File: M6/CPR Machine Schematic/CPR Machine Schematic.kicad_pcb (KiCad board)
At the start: 2 copper layers, 79.8 x 56.3 mm, 72 parts, among them J1 Battery 22.2V IN, J10 Stop Button Port, J11 Go Button Port, J12 I2C Port, J13 Raspberry_Pi_2_3, J2 5V Spare Headers, J3 Power Switch, J4 3V3 Spare Headers, J5 12 Spare headers, J6 Battery Spare headers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

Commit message: Final PCB
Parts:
- removed the REF** at (118.6, 76.0)
- removed the REF** at (176.6, 125.0)
- removed the REF** at (118.6, 125.0)
- removed the REF** at (176.6, 76.0)
- added G***: LOGO, Images:MIT, F.Cu at (149.6, 89.2)
- added H1: MountingHole, MountingHole:MountingHole_2.7mm_M2.5_Pad, F.Cu at (176.6, 76.0)
- added H2: MountingHole, MountingHole:MountingHole_2.7mm_M2.5_Pad, F.Cu at (176.6, 125.0)
- added H3: MountingHole, MountingHole:MountingHole_2.7mm_M2.5_Pad, F.Cu at (118.6, 76.0)
- added H4: MountingHole, MountingHole:MountingHole_2.7mm_M2.5_Pad, F.Cu at (118.6, 125.0)
- F1: value 5A -> 4A
- J9: footprint Connector_PinHeader_2.54mm:PinHeader_1x02_P2.54mm_Vertical -> TerminalBlock:TerminalBlock_MaiXu_MX126-5.0-02P_1x02_P5.00mm
- Q2: value AO3407A -> SSM3J332R
- R16: value 80.6 Ohm -> 80.6 kOhm
- R6: value TEMP kOhm -> 0 Ohm; footprint Resistor_SMD:R_1206_3216Metric -> Resistor_SMD:R_1206_3216Metric_Pad1.30x1.75mm_HandSolder
- REF**: moved to F.Cu
- moved G*** 25.2 mm to (170.2, 90.8)
- moved REF** 9.23 mm to (164.8, 83.2), turned to 0 degrees
- moved REF** 7.21 mm to (159.6, 89.1)
- moved J9 4.67 mm to (189.8, 82.8), turned to 90 degrees
- moved J11 1.23 mm to (185.1, 95.8)
- moved R6 1.00 mm to (180.4, 85.5), turned to 90 degrees
- moved R15 0.25 mm to (181.0, 98.5)
- moved R11 0.05 mm to (139.7, 84.3)
- moved R3 0.05 mm to (140.8, 106.1)
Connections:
- R6 pad 1: Net-(J9-Pin_2) -> +3.3V
- R6 pad 2: +5V -> Net-(J9-Pin_2)
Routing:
- net +3.3V: track 64.8 -> 96.6 mm, vias 1 -> 2
- net Net-(J9-Pin_2): track 6.59 -> 11.9 mm
- net Net-(J9-Pin_1): track 9.98 -> 12.5 mm
- net Net-(U2-FB): track 27.1 -> 29.0 mm
- net +5V: track 12.2 -> 10.7 mm, vias 22 -> 21
- net /HMI_Raspi/Go LED Power: track 12.4 -> 11.2 mm
- net /HMI_Raspi/Go Button Ground: track 15.6 -> 14.8 mm
- net +22.2V: track 133.2 -> 134.1 mm
- net /HMI_Raspi/Go Button: track 76.5 -> 76.0 mm
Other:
- board text added: "Battery - 5V Buck"
- board text added: "L+"
- board text added: "L-"
- board text added: "{dblquote}Can we get rid of Canada?{dblquote}"
- board text removed: "*Logo Space* *Ideas Appreciated*"
- board text removed: "Battery - 12V Buck"
- board text removed: "Laser +"
- board text removed: "Laser -"

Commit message: Start of Board V2
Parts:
- added J15: Conn_02x20_Odd_Even, Connector_PinHeader_2.54mm:PinHeader_2x20_P2.54mm_Vertical, F.Cu at (171.9, 130.5)
- moved F2 48.4 mm to (173.2, 119.4)
- moved J13 48.3 mm to (171.8, 123.7), turned to 90 degrees
- moved J12 2.58 mm to (185.1, 126.3), turned to 180 degrees
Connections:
- J13 pad 10: unconnected-(J13-GPIO15/RXD-Pad10) -> /Raspi/GPIO15
- J13 pad 11: unconnected-(J13-GPIO17-Pad11) -> /Raspi/GPIO17
- J13 pad 12: unconnected-(J13-GPIO18/PWM0-Pad12) -> /Raspi/GPIO18
- J13 pad 13: unconnected-(J13-GPIO27-Pad13) -> /Raspi/GPIO27
- J13 pad 15: unconnected-(J13-GPIO22-Pad15) -> /Raspi/GPIO22
- J13 pad 19: unconnected-(J13-MOSI0/GPIO10-Pad19) -> /Raspi/GPIO10
- J13 pad 21: unconnected-(J13-MISO0/GPIO9-Pad21) -> /Raspi/GPIO9
- J13 pad 23: unconnected-(J13-SCLK0/GPIO11-Pad23) -> /Raspi/GPIO11
- J13 pad 24: unconnected-(J13-~{CE0}/GPIO8-Pad24) -> /Raspi/GPIO8
- J13 pad 26: unconnected-(J13-~{CE1}/GPIO7-Pad26) -> /Raspi/GPIO7
- J13 pad 27: unconnected-(J13-ID_SD/GPIO0-Pad27) -> /Raspi/GPIO0
- J13 pad 28: unconnected-(J13-ID_SC/GPIO1-Pad28) -> /Raspi/GPIO1
- J13 pad 29: unconnected-(J13-GCLK1/GPIO5-Pad29) -> /Raspi/GPIO5
- J13 pad 31: unconnected-(J13-GCLK2/GPIO6-Pad31) -> /Raspi/GPIO6
- J13 pad 33: unconnected-(J13-PWM1/GPIO13-Pad33) -> /Raspi/GPIO13
- J13 pad 35: unconnected-(J13-GPIO19/MISO1-Pad35) -> /Raspi/GPIO19
- J13 pad 36: unconnected-(J13-GPIO16-Pad36) -> /Raspi/GPIO16
- J13 pad 38: unconnected-(J13-GPIO20/MOSI1-Pad38) -> /Raspi/GPIO20
- J13 pad 40: unconnected-(J13-GPIO21/SCLK1-Pad40) -> /Raspi/GPIO21
- J13 pad 7: unconnected-(J13-GCLK0/GPIO4-Pad7) -> /Raspi/GPIO4
- J13 pad 8: unconnected-(J13-GPIO14/TXD-Pad8) -> /Raspi/GPIO14
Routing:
- net +3.3V: track 96.6 -> 189.8 mm, vias 2 -> 3
- net /HMI_Raspi/Stop_Enable: track 34.9 -> 93.9 mm, vias 2 -> 5
- net /Raspi/I2C_SDA: track 67.4 -> 24.2 mm, vias 1 -> 2
- net /Raspi/I2C_SCL: track 68.0 -> 26.4 mm, vias 1 -> 2
- net /HMI_Raspi/Laser_PWM: track 56.7 -> 91.0 mm, vias 4 -> 3
- net GND: track 39.1 -> 69.6 mm, vias 9 -> 8
- net /HMI_Raspi/Go Button: track 76.0 -> 66.1 mm, vias 1 -> 3
- net /HMI_Raspi/Go_Enable: track 64.4 -> 73.6 mm, vias 4 -> 5
- net /Raspi/GPIO1: track 0.00 -> 7.77 mm
- net /Raspi/GPIO5: track 0.00 -> 7.77 mm
- net /Raspi/GPIO9: track 0.00 -> 7.77 mm
- net /Raspi/GPIO4: track 0.00 -> 7.77 mm
- net /Raspi/GPIO22: track 0.00 -> 7.77 mm
- net /Raspi/GPIO18: track 0.00 -> 7.77 mm
- net /Raspi/GPIO21: track 0.00 -> 7.77 mm
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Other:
- board size 79.8 x 56.3 mm -> 79.8 x 62.8 mm
- board text added: "Daniel Gliksberg HB Main Board v2 2.679"
- board text removed: "Daniel Gliksberg HB Main Board v1 2.679"

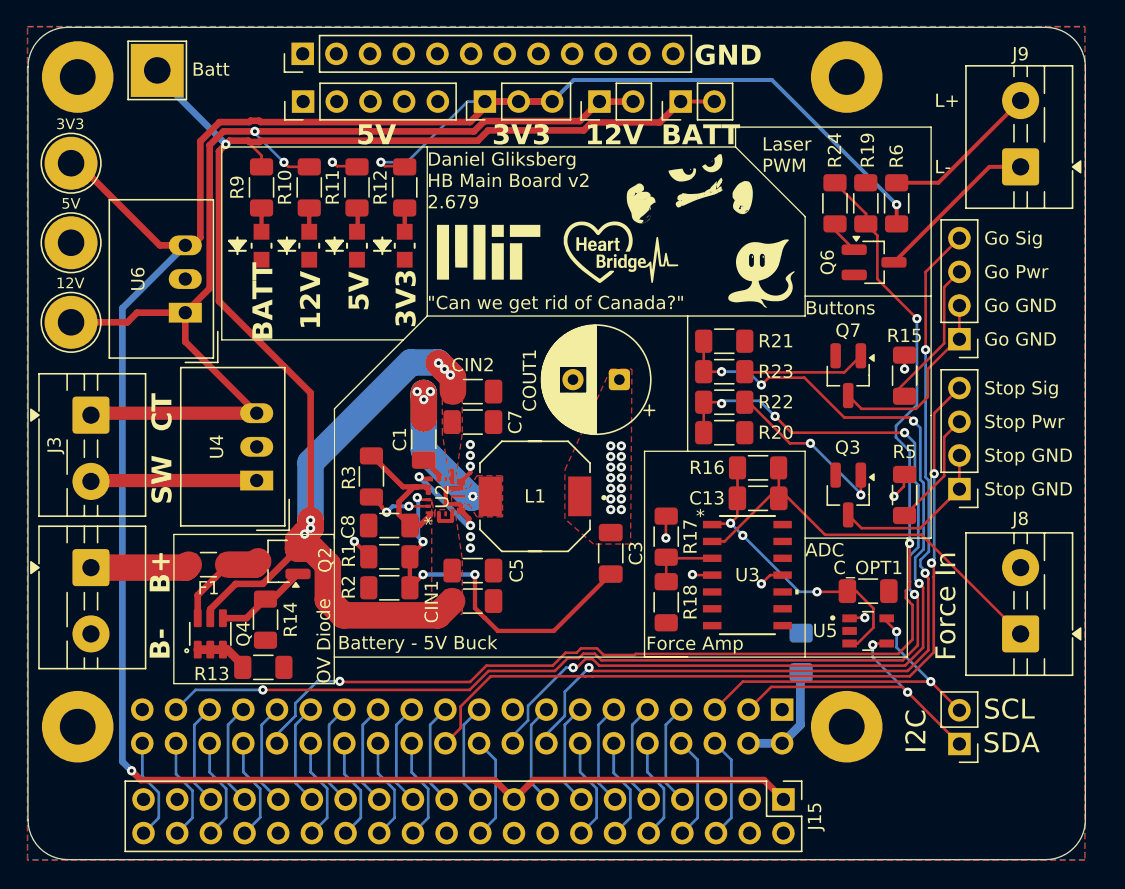
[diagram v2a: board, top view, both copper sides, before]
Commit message: Fixed edge cuts
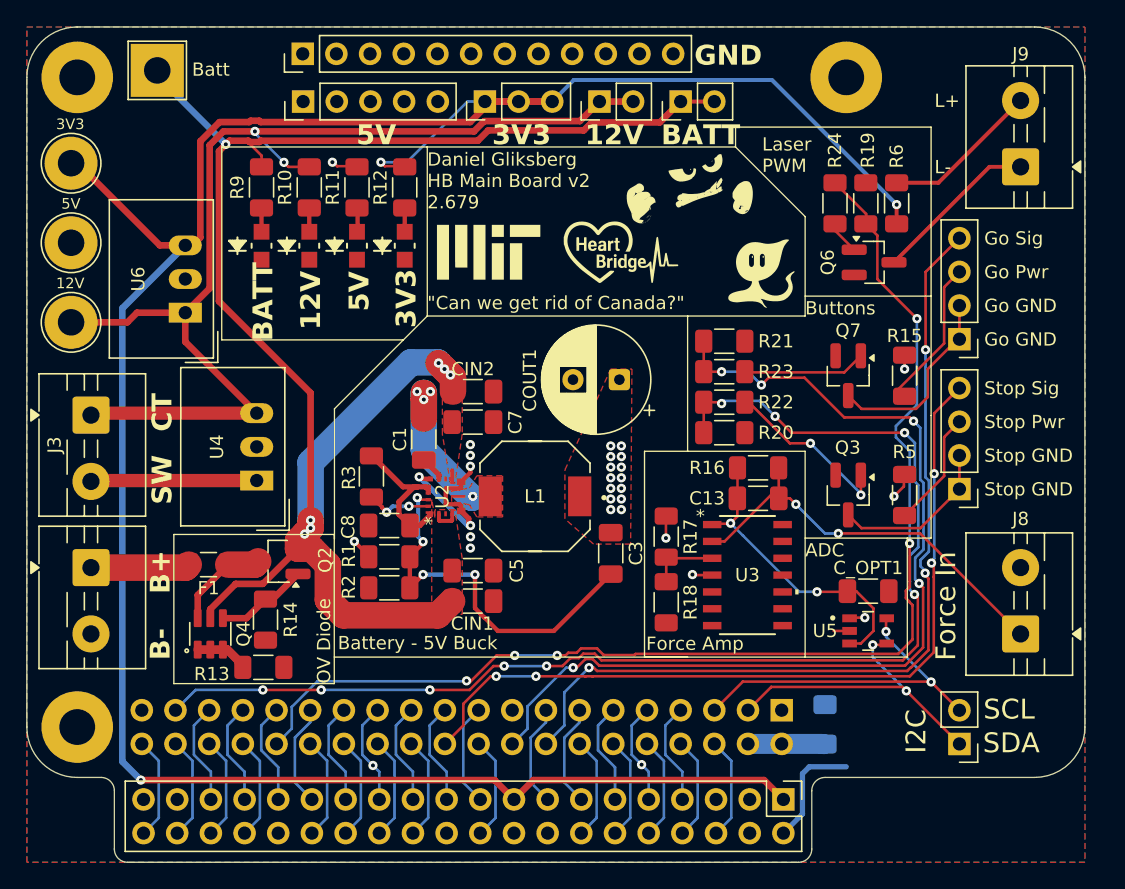
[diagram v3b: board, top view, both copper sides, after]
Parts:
- removed H2: MountingHole, MountingHole:MountingHole_2.7mm_M2.5_Pad
- moved F2 5.69 mm to (175.0, 124.8)
- moved J13 0.06 mm to (171.7, 123.7)
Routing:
- net +5V: track 11.1 -> 19.7 mm
- net Net-(F2-Pad2): track 8.47 -> 5.82 mm
- net GND: track 69.6 -> 68.7 mm, vias 8 -> 9
- net Net-(J8-Pin_1): track 31.6 -> 31.4 mm, vias 0 -> 2
- net Net-(U5-AIN): track 23.0 -> 23.2 mm, vias 3 -> 2
- net /HMI_Raspi/Laser_PWM: track 91.0 -> 91.1 mm, vias 3 -> 5
- net /HMI_Raspi/Stop Button: vias 2 -> 4
- net /HMI_Raspi/Stop_Enable: track 93.9 -> 94.0 mm, vias 5 -> 9
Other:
- board size 79.8 x 62.8 mm -> 79.8 x 63 mm

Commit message: Board V2
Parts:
- added COUT2: 23.7 uF, Capacitor_SMD:C_1210_3225Metric_Pad1.33x2.70mm_HandSolder, F.Cu at (158.1, 101.1)
- added Q5: DMMT5401 PNP, 2679:SOT95P285X140-6N, F.Cu at (162.7, 99.2)
- added Q8: DMG2305UX-EV, Package_TO_SOT_SMD:SOT-23_Handsoldering, F.Cu at (163.2, 104.5)
- added R25: 10 kOhm, Resistor_SMD:R_1206_3216Metric_Pad1.30x1.75mm_HandSolder, F.Cu at (158.2, 97.0)
- added R26: 47 kOhm, Resistor_SMD:R_1206_3216Metric_Pad1.30x1.75mm_HandSolder, F.Cu at (158.2, 94.6)
- COUT1: value 47 uF -> 23.7 uF; footprint Capacitor_THT:CP_Radial_D8.0mm_P3.50mm -> Capacitor_SMD:C_1210_3225Metric_Pad1.33x2.70mm_HandSolder
- moved COUT1 14.4 mm to (158.1, 113.1)
- moved C3 4.59 mm to (161.8, 115.4)
- moved R3 3.62 mm to (142.2, 109.4), turned to 180 degrees
- moved R20 2.22 mm to (169.6, 102.8)
- moved R21 2.22 mm to (169.6, 95.9)
- moved R22 2.22 mm to (169.6, 100.5)
- moved R23 2.22 mm to (169.6, 98.2)
- moved CIN2 2.10 mm to (149.8, 98.1)
- moved R2 2.02 mm to (142.2, 116.5)
- moved R1 2.01 mm to (142.2, 114.2)
- moved C8 1.99 mm to (142.2, 111.8)
- moved U2 1.82 mm to (145.1, 108.9)
- moved R16 1.75 mm to (171.7, 105.4)
- moved C13 1.75 mm to (171.7, 107.8)
- moved R17 1.68 mm to (164.7, 110.7)
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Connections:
- C3 pad 2: +5V -> /Power/Reg OUT
- COUT1 pad 1: +5V -> /Power/Reg OUT
- L1 pad 1: +5V -> /Power/Reg OUT
- R1 pad 1: +5V -> /Power/Reg OUT
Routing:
- net /Power/Reg OUT: track 0.00 -> 31.6 mm, vias 0 -> 4
- net Net-(Q5-Pad4): track 0.00 -> 14.8 mm
- net GND: track 68.7 -> 79.4 mm, vias 9 -> 46
- net /Power/LX: track 11.9 -> 1.41 mm
- net Net-(U2-FB): track 29.0 -> 34.3 mm
- net Net-(Q5-Pad1): track 0.00 -> 4.34 mm
- net Net-(U2-BIAS): track 11.7 -> 15.4 mm
- net /HMI_Raspi/Go_Enable: track 73.7 -> 70.3 mm, vias 5 -> 4
- net +5V: track 19.7 -> 22.7 mm, vias 21 -> 30
- net /HMI_Raspi/Stop_Enable: track 94.0 -> 91.3 mm, vias 9 -> 5
- net Net-(U2-PGOOD): track 4.99 -> 2.62 mm, vias 2 -> 0
- net Net-(Q7-G): track 9.29 -> 7.07 mm
- net Net-(Q3-G): track 13.2 -> 11.2 mm, vias 2 -> 0
- net Net-(U5-AIN): track 23.2 -> 21.5 mm
- net Net-(J8-Pin_1): track 31.4 -> 29.7 mm
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- added copper zone on B.Cu, net /Power/LX
- added copper zone on F.Cu, net /Power/Reg OUT
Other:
- board text added: "Daniel Gliksberg HB Main Board v2"
- board text removed: "Daniel Gliksberg HB Main Board v2 2.679"

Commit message: Board V2 Final
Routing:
- net +22.2V: track 133.4 -> 133.1 mm, vias 7 -> 8
